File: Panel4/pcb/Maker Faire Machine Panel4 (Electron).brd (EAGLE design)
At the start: 58.4 x 63.5 mm, 26 parts, among them IC1 TJA1049

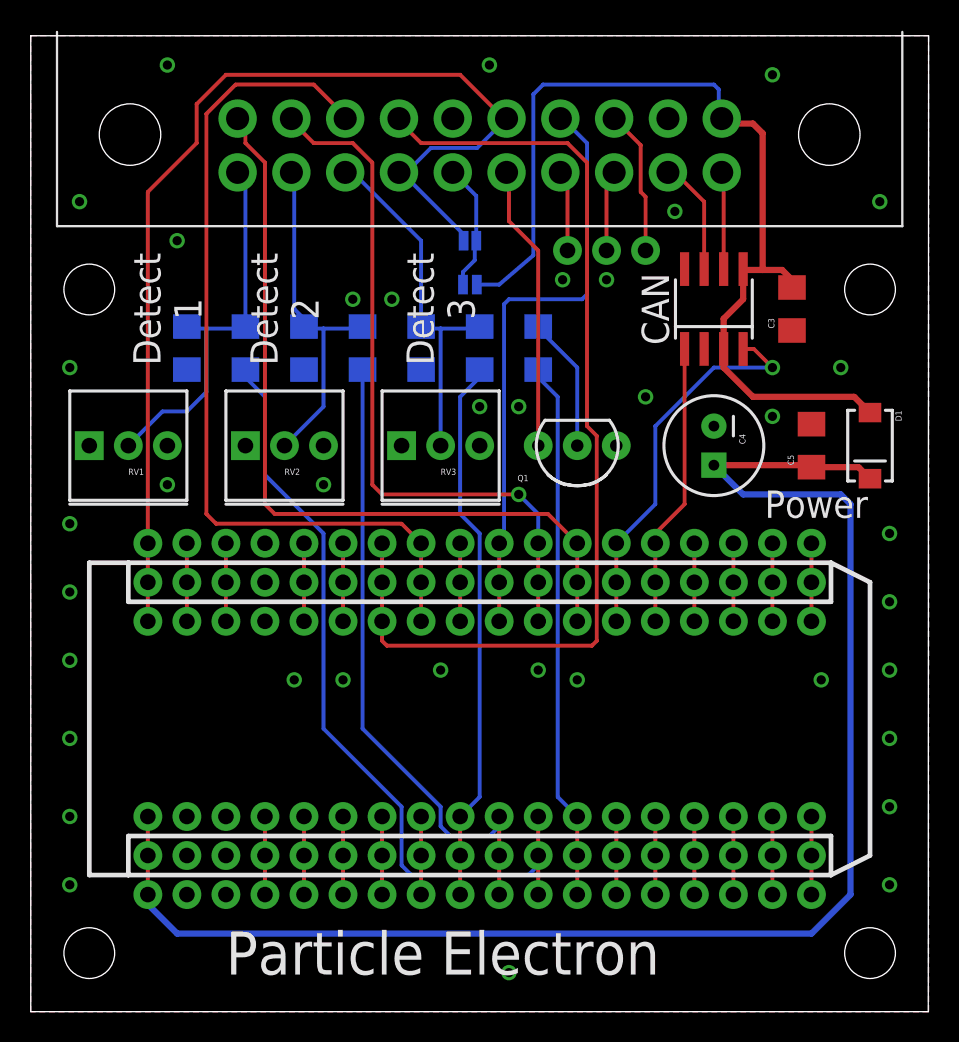
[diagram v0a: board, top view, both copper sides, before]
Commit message: First version of panel 4 PCB done
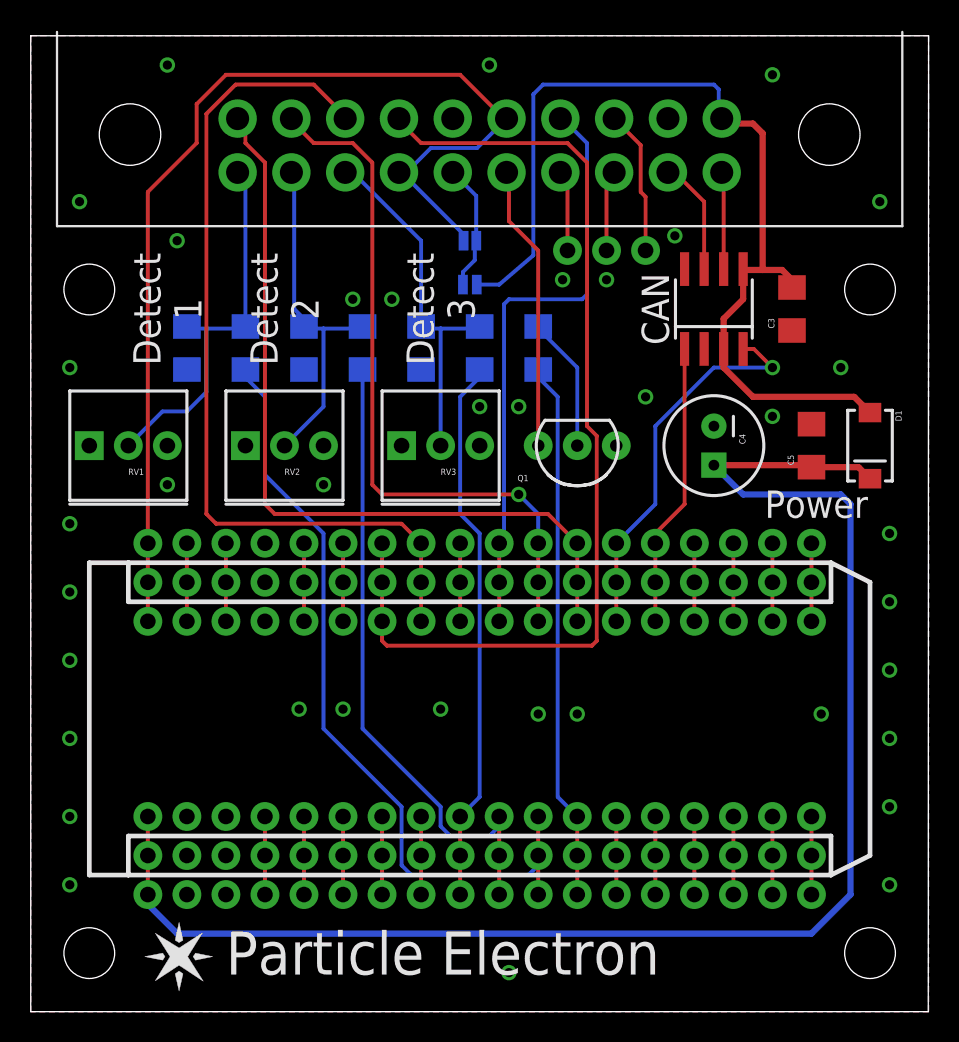
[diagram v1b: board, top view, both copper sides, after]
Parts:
- U$2: value SPARK_LOGO.. -> SPARK_LOGOSILK; device Spark:SPARK_LOGO -> Spark:SPARK_LOGO_SILK
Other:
- board text added: "3V3 RST VBAT GND D7 D6 D5 D4 D3 D2 D1 D0 C5 C4 C3 C2 C1 C0"
- board text added: "VIN GND TX RX WKP DAC A5 A4 A3 A2 A1 A0 B5 B4 B3 B2 B1 B0"
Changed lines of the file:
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@@
 <layer number="14" name="Route14" color="1" fill="6" visible="no" active="no"/>
 <layer number="15" name="Route15" color="4" fill="6" visible="no" active="no"/>
-<layer number="16" name="Bottom" color="1" fill="1" visible="yes" active="yes"/>
+<layer number="16" name="Bottom" color="1" fill="1" visible="no" active="yes"/>
 <layer number="17" name="Pads" color="2" fill="1" visible="yes" active="yes"/>
 <layer number="18" name="Vias" color="2" fill="1" visible="yes" active="yes"/>
@@
 <layer number="20" name="Dimension" color="15" fill="1" visible="yes" active="yes"/>
 <layer number="21" name="tPlace" color="7" fill="1" visible="yes" active="yes"/>
-<layer number="22" name="bPlace" color="7" fill="1" visible="yes" active="yes"/>
+<layer number="22" name="bPlace" color="7" fill="1" visible="no" active="yes"/>
 <layer number="23" name="tOrigins" color="15" fill="1" visible="yes" active="yes"/>
-<layer number="24" name="bOrigins" color="15" fill="1" visible="yes" active="yes"/>
+<layer number="24" name="bOrigins" color="15" fill="1" visible="no" active="yes"/>
 <layer number="25" name="tNames" color="7" fill="1" visible="yes" active="yes"/>
-<layer number="26" name="bNames" color="7" fill="1" visible="yes" active="yes"/>
+<layer number="26" name="bNames" color="7" fill="1" visible="no" active="yes"/>
 <layer number="27" name="tValues" color="7" fill="1" visible="no" active="yes"/>
 <layer number="28" name="bValues" color="7" fill="1" visible="no" active="yes"/>
 <layer number="29" name="tStop" color="7" fill="3" visible="yes" active="yes"/>
-<layer number="30" name="bStop" color="7" fill="6" visible="yes" active="yes"/>
+<layer number="30" name="bStop" color="7" fill="6" visible="no" active="yes"/>
 <layer number="31" name="tCream" color="7" fill="4" visible="yes" active="yes"/>
-<layer number="32" name="bCream" color="7" fill="5" visible="yes" active="yes"/>
+<layer number="32" name="bCream" color="7" fill="5" visible="no" active="yes"/>
 <layer number="33" name="tFinish" color="6" fill="3" visible="no" active="yes"/>
 <layer number="34" name="bFinish" color="6" fill="6" visible="no" active="yes"/>
@@
 <layer number="38" name="bTest" color="7" fill="1" visible="no" active="yes"/>
 <layer number="39" name="tKeepout" color="4" fill="11" visible="yes" active="yes"/>
-<layer number="40" name="bKeepout" color="1" fill="11" visible="yes" active="yes"/>
-<layer number="41" name="tRestrict" color="4" fill="10" visible="no" active="yes"/>
+<layer number="40" name="bKeepout" color="1" fill="11" visible="no" active="yes"/>
+<layer number="41" name="tRestrict" color="4" fill="10" visible="yes" active="yes"/>
 <layer number="42" name="bRestrict" color="1" fill="10" visible="no" active="yes"/>
 <layer number="43" name="vRestrict" color="2" fill="10" visible="no" active="yes"/>
@@
 <text x="29.845" y="49.53" size="1.27" layer="22" rot="MR0" align="bottom-right">3.3V</text>
 <text x="29.845" y="46.99" size="1.27" layer="22" rot="MR0" align="bottom-right">5V</text>
-<text x="26.67" y="46.99" size="1.27" layer="22" rot="MR0">Laser
+<text x="26.67" y="47.3075" size="1.27" layer="22" rot="MR0">Laser
 VCC</text>
 <text x="13.335" y="53.0225" size="1.016" layer="22" rot="MR0" align="top-center">SIG1</text>
@@
 <text x="16.8275" y="60.6425" size="1.016" layer="22" rot="MR0" align="top-center">SCL</text>
 <text x="13.335" y="60.6425" size="1.016" layer="22" rot="MR0" align="top-center">SDA</text>
+<text x="51.435" y="14.2875" size="1.27" layer="22" distance="100" rot="SMR270" align="bottom-right">VIN
+GND
+TX
+RX
+WKP
+DAC
+A5
+A4
+A3
+A2
+A1
+A0
+B5
+B4
+B3
+B2
+B1
+B0</text>
+<text x="51.435" y="23.495" size="1.27" layer="22" distance="100" rot="SMR270">3V3
+RST
+VBAT
+GND
+D7
+D6
+D5
+D4
+D3
+D2
+D1
+D0
+C5
+C4
+C3
+C2
+C1
+C0</text>
 </plain>
 <attributes>
@@
 <element name="JP1" library="panel4" package="2X10_MOLEX_MX150" value="" x="29.21" y="54.61" smashed="yes" rot="R180">
 <attribute name="VALUE" x="11.43" y="49.53" size="1.27" layer="27" rot="R180"/>
+<attribute name="PARTNO" value="348302001" x="29.21" y="54.61" size="1.778" layer="27" rot="R180" display="off"/>
 </element>
 <element name="ELECTRON" library="Particle-Devices" package="ELECTRON_STACKABLE" value="ELECTRON_WITH_STACKABLE_HEADERS" x="54.61" y="8.89" smashed="yes" rot="R90">
@@
 <attribute name="BOM" value="EXCLUDE" x="-2.54" y="34.29" size="1.778" layer="27" display="off"/>
 </element>
-<element name="U$2" library="Spark" package="SPARK_LOGO" value="SPARK_LOGO.." x="7.366" y="1.27"/>
+<element name="U$2" library="Spark" package="SPARK_LOGO_SILK" value="SPARK_LOGOSILK" x="7.366" y="1.27">
+<attribute name="BOM" value="EXCLUDE" x="7.366" y="1.27" size="1.778" layer="27" display="off"/>
+</element>
 <element name="JP2" library="SparkFun-Connectors" package="1X03_NO_SILK" value="" x="40.005" y="49.53" smashed="yes" rot="R180">
 <attribute name="VALUE" x="41.275" y="52.705" size="1.27" layer="27" rot="R180"/>
+<attribute name="DNP" value="T" x="40.005" y="49.53" size="1.778" layer="27" rot="R180" display="off"/>
 </element>
 </elements>
@@
 <via x="52.705" y="41.91" extent="1-16" drill="0.6"/>
 <via x="55.88" y="31.115" extent="1-16" drill="0.6"/>
-<via x="33.02" y="22.225" extent="1-16" drill="0.6"/>
-<via x="26.67" y="22.225" extent="1-16" drill="0.6"/>
-<via x="20.32" y="21.59" extent="1-16" drill="0.6"/>
-<via x="17.145" y="21.59" extent="1-16" drill="0.6"/>
-<via x="35.56" y="21.59" extent="1-16" drill="0.6"/>
-<via x="51.435" y="21.59" extent="1-16" drill="0.6"/>
+<via x="33.02" y="19.3675" extent="1-16" drill="0.6"/>
+<via x="26.67" y="19.685" extent="1-16" drill="0.6"/>
+<via x="20.32" y="19.685" extent="1-16" drill="0.6"/>
+<via x="17.4625" y="19.685" extent="1-16" drill="0.6"/>
+<via x="35.56" y="19.3675" extent="1-16" drill="0.6"/>
+<via x="51.435" y="19.3675" extent="1-16" drill="0.6"/>
 <via x="55.88" y="22.225" extent="1-16" drill="0.6"/>
 <via x="55.88" y="26.67" extent="1-16" drill="0.6"/>
@@
 <via x="48.26" y="60.96" extent="1-16" drill="0.6"/>
 <via x="55.245" y="52.705" extent="1-16" drill="0.6"/>
-<via x="41.91" y="52.07" extent="1-16" drill="0.6"/>
+<via x="41.91" y="50.4825" extent="1-16" drill="0.6"/>
 <via x="34.6075" y="47.625" extent="1-16" drill="0.6"/>
 <via x="29.845" y="61.595" extent="1-16" drill="0.6"/>
